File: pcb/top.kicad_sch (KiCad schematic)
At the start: 67 parts, among them J1 Conn_01x01, J10 Conn_01x01, J11 Conn_01x01, J2 Conn_01x01, J3 Conn_01x06, J4 Conn_01x01, J5 Conn_01x01, J6 Conn_01x01, J7 Conn_01x01, J8 Conn_01x01, J9 Conn_01x01, Q1 2N7002, Q2 2N7002, Q3 2N7002, Q4 2N7002, U1 L78L05_SOT89, U2 PIC12F629-ISN

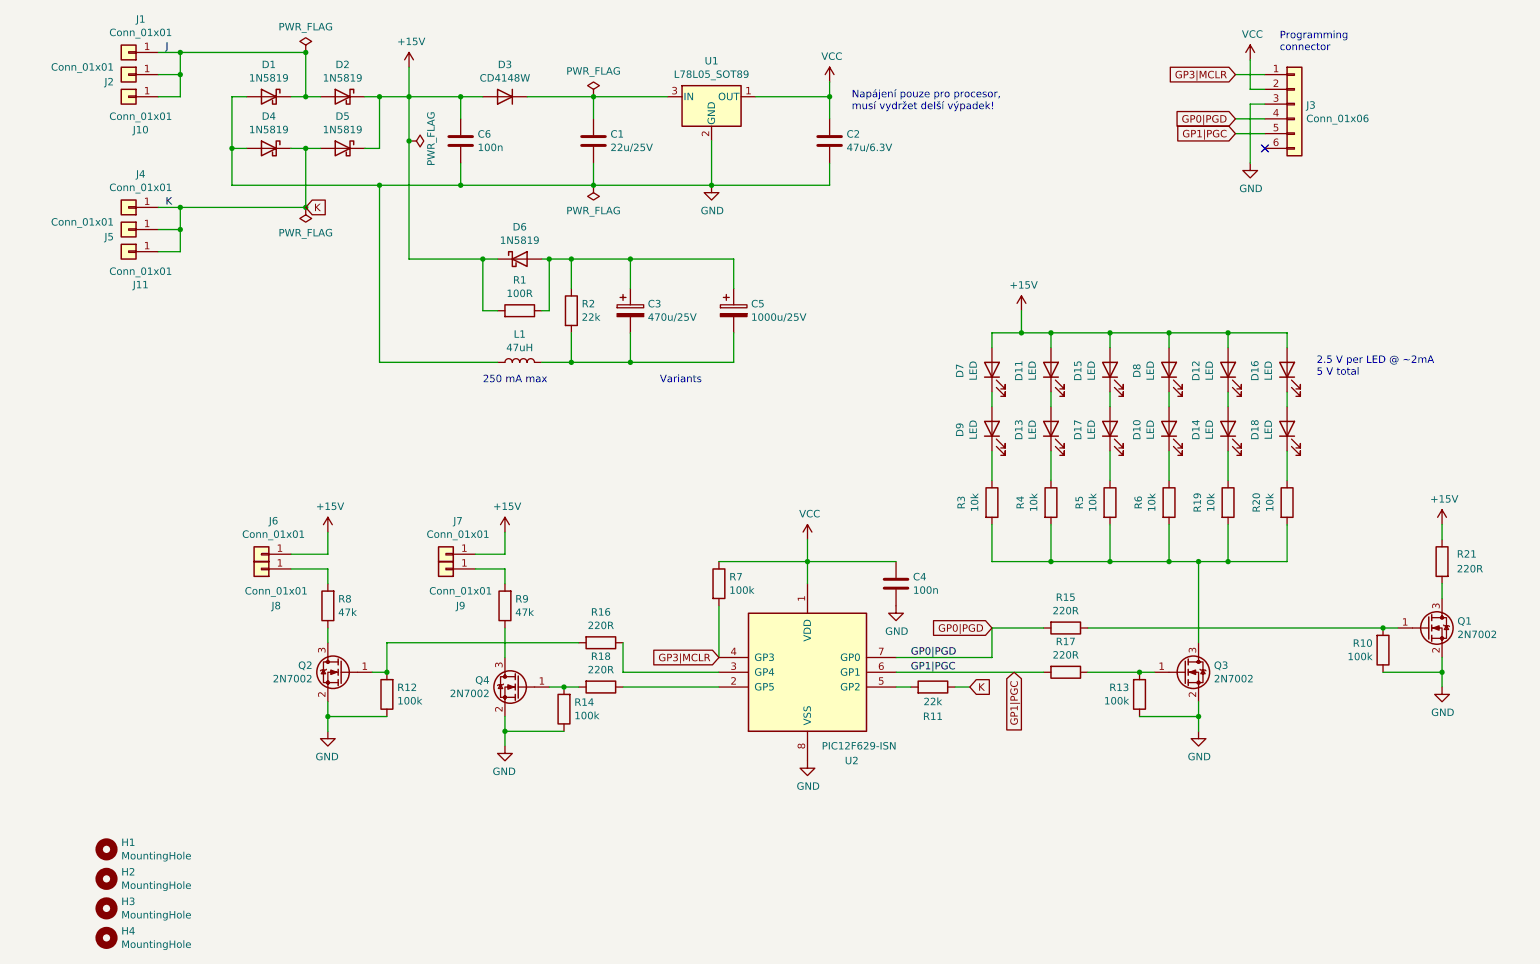
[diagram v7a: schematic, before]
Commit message: Use 8V stabilized for LEDs.
To keep LEDs longer running on capacitor while maintaining brightness.
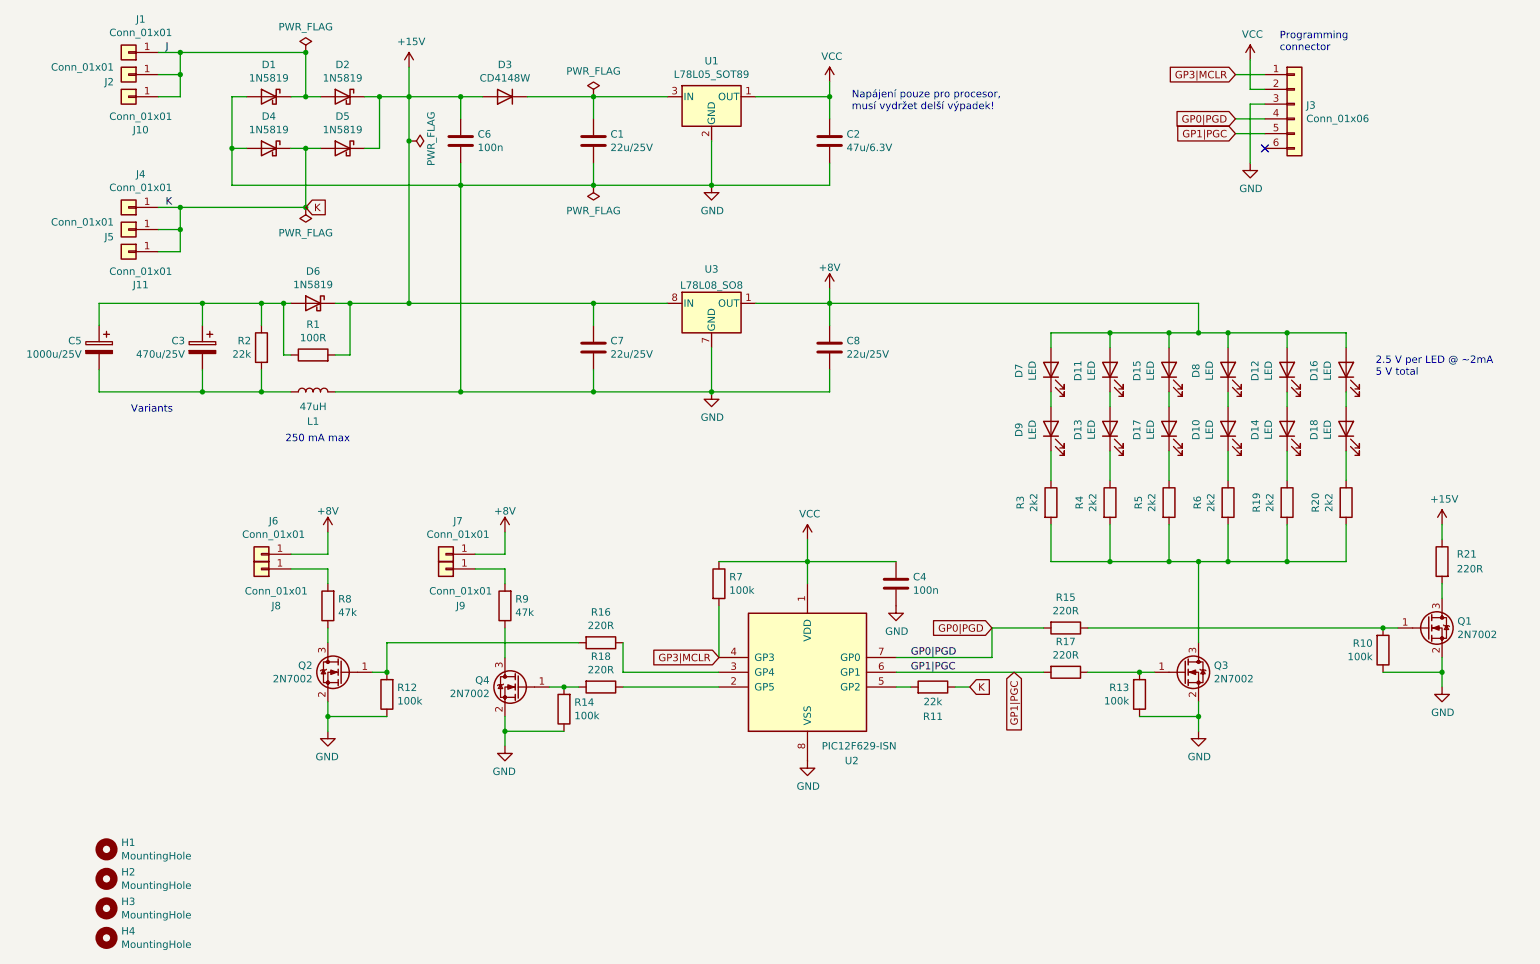
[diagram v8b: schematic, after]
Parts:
- added C7, C8: 22u/25V, Capacitor_SMD:C_0805_2012Metric_Pad1.18x1.45mm_HandSolder, symbol Device:C
- added U3: L78L08_SO8, Package_SO:SOIC-8_3.9x4.9mm_P1.27mm, symbol Regulator_Linear:L78L08_SO8
- R19, R20, R3, R4, R5, R6: value 10k -> 2k2; LCSC C17414 -> C17520
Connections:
- net +15V: now also C7.1, U3.8 (IN); no longer D11.2 (A), D12.2 (A), D15.2 (A), D16.2 (A), D7.2 (A), D8.2 (A), J6.1 (Pin_1), J7.1 (Pin_1)
- net GND: now also C7.2, C8.2, U3.2 (GND), U3.3 (GND), U3.6 (GND), U3.7 (GND)
- new net +8V: C8.1, D11.2 (A), D12.2 (A), D15.2 (A), D16.2 (A), D7.2 (A), D8.2 (A), J6.1 (Pin_1), J7.1 (Pin_1), U3.1 (OUT)
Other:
- moved on the sheet: C3, C5, D10, D11, D12, D13, D14, D15, D16, D17, D18, D6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
